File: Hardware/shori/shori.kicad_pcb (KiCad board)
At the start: 4 copper layers, 106 x 44.8 mm, 134 parts, among them J1 430450200, J2 SWD_Header, J3 UART_Header, J4 530480310, J5 Conn_01x03, J6 530480210, J7 GROUND PROBE, SW1 SW_SPDT, U1 CS4272, U2 STM32H750VBTx, U3 NE5532, U4 NE5532, U5 TPS73733DCQR, U6 W25Q128JVS, U7 TLV9001IDCK, U8 MAX40200AUK, Y1 16MHz

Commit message: Shori: Final BOM touches
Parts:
- C15: footprint MyFootprints:CAPPM3216X180N -> Capacitor_SMD:C_1206_3216Metric_Pad1.33x1.80mm_HandSolder
- C19, C35: value 1μF -> 1uF
- C21, C34: value 0.1uF -> 100nF
- moved G*** 0.68 mm to (156.6, 92.9)
- moved C15 0.25 mm to (156.0, 128.5)
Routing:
- net GND: track 67.6 -> 71.6 mm, vias 117 -> 118
- net +5V: track 8.97 -> 9.50 mm

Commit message: Gen: PSU, rev 1 schems done, mae and shori orderd
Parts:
- AUDIO IN: renamed from J4
- AUDIO OUT: renamed from J6
- AUX IN: renamed from J5
- moved H1 2.75 mm to (195.2, 130.5)
- moved H2 2.75 mm to (195.0, 96.0)
- moved GND 2.28 mm to (104.0, 122.2)
- moved H3 1.79 mm to (103.8, 130.5)
- moved H4 1.79 mm to (103.8, 95.8)
- moved C50 1.00 mm to (170.5, 111.8)
- renumbered TP2 to 3V3, TP3 to 3V3A, TP1 to 5V, TP4 to 5VA, J7 to GND, TP5 to MCK, SW1 to P, J1 to POWER, J2 to PROGRAMMING, RST1 to RST, TP6 to TX, J3 to UART
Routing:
- net GND: track 71.6 -> 101.1 mm, vias 118 -> 146
- net +5VA: track 66.7 -> 67.7 mm
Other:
- board size 106 x 44.8 mm -> 101.5 x 44.8 mm

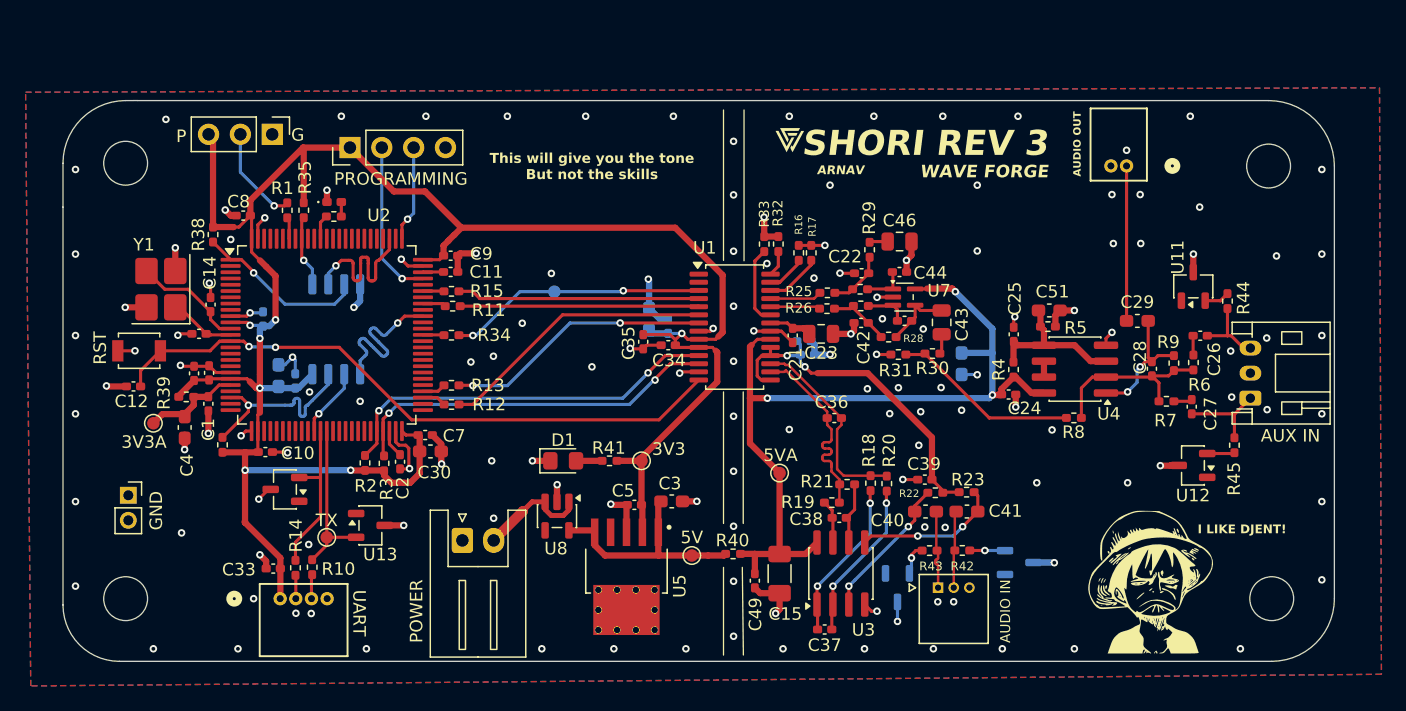
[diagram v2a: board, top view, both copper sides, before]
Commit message: Remvoed 3.3V on shori UART and changed tantalum cap
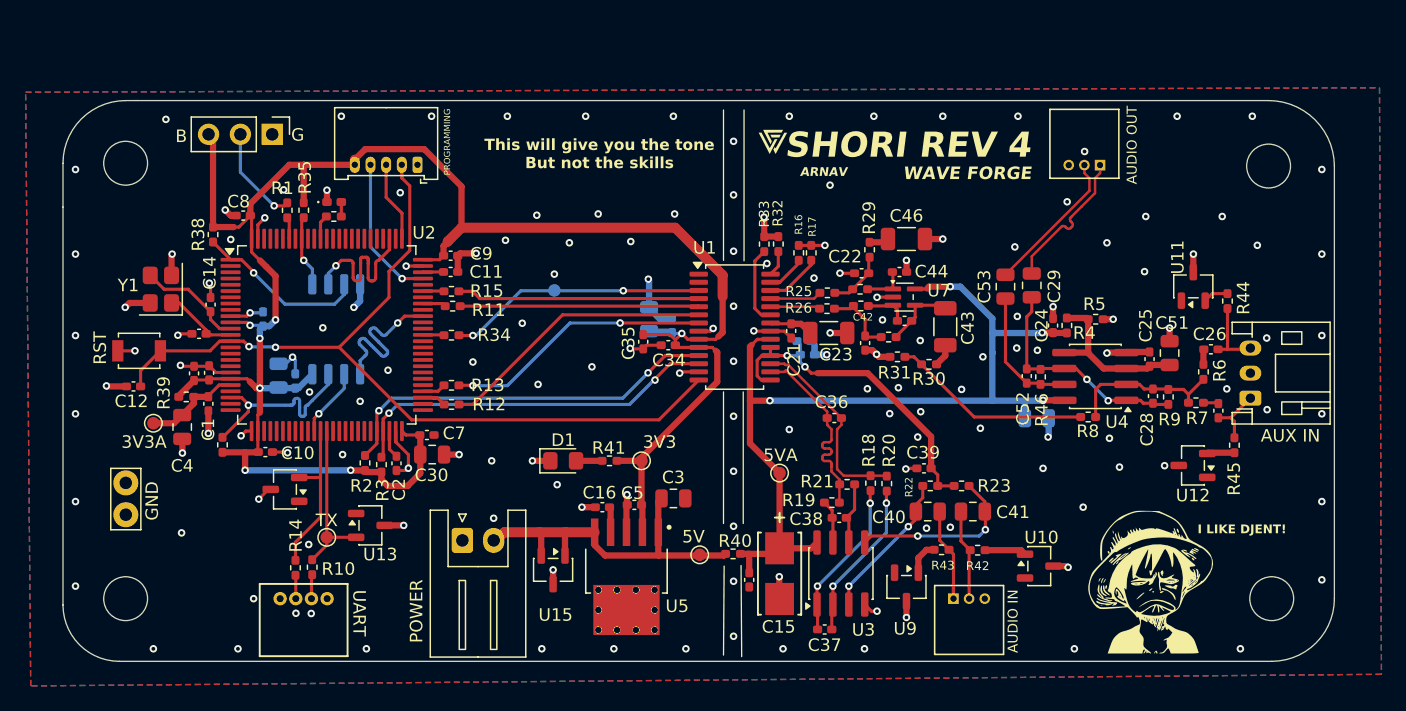
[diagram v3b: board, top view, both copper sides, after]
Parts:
- removed the AUDIO OUT at (183.7, 96.0)
- removed C33: 100nF, Capacitor_SMD:C_0402_1005Metric_Pad0.74x0.62mm_HandSolder
- removed the GND at (104.0, 122.2)
- removed the PROGRAMMING at (121.7, 94.5)
- removed U8: MAX40200AUK, Package_TO_SOT_SMD:SOT-23-5
- added AUDIO OUT: 530480310, MyFootprints:MOLEX_530480310, F.Cu at (181.6, 95.9)
- added C16: 10nF, Capacitor_SMD:C_0402_1005Metric_Pad0.74x0.62mm_HandSolder, F.Cu at (141.8, 123.2)
- added C52: 100pF, Capacitor_SMD:C_0402_1005Metric_Pad0.74x0.62mm_HandSolder, F.Cu at (175.7, 112.7)
- added C53: 10uF, Capacitor_SMD:C_0805_2012Metric, F.Cu at (174.0, 105.6)
- added GND: TestPoint_Bridge_Pitch2.54mm_Drill1.0mm, TestPoint:TestPoint_Bridge_Pitch2.54mm_Drill1.0mm, F.Cu at (103.8, 123.8)
- added PROGRAMMING: Conn_01x05_Pin, Connector_Molex:Molex_PicoBlade_53048-0510_1x05_P1.25mm_Horizontal, F.Cu at (127.1, 95.9)
- added R46: 10K, Resistor_SMD:R_0402_1005Metric_Pad0.72x0.64mm_HandSolder, F.Cu at (176.8, 112.8)
- added U15: ~, Package_TO_SOT_SMD:SOT-23-3, F.Cu at (137.9, 128.2)
- C15: value 100uF -> 47uF; footprint Capacitor_SMD:C_1206_3216Metric_Pad1.33x1.80mm_HandSolder -> MyFootprints:CAPMP6.3X3.2_2.8N_KEM
- C17, C29, C3, C30, C4, C40, C41, C47, C50, C51: footprint Capacitor_SMD:C_0603_1608Metric_Pad1.08x0.95mm_HandSolder -> Capacitor_SMD:C_0805_2012Metric
- C23, C43, C46: footprint Capacitor_SMD:C_0805_2012Metric -> Capacitor_SMD:C_1206_3216Metric
- U10, U9: moved to F.Cu
- Y1: value 16MHz -> 12.288MHz; footprint Crystal:Crystal_SMD_3225-4Pin_3.2x2.5mm_HandSoldering -> Crystal:Crystal_SMD_3225-4Pin_3.2x2.5mm
- moved C25 11.0 mm to (185.5, 111.4)
- moved C51 10.2 mm to (187.1, 110.9), turned to -90 degrees
- moved C29 8.89 mm to (176.1, 105.5), turned to 90 degrees
- moved C50 7.41 mm to (176.5, 116.1), turned to 180 degrees
- moved C24 6.55 mm to (177.8, 108.7), turned to 90 degrees
- moved R4 5.52 mm to (178.9, 108.7)
- moved R5 3.86 mm to (181.2, 108.2)
- moved R9 2.74 mm to (187.0, 114.4), turned to -90 degrees
- moved R7 2.36 mm to (189.2, 114.9)
- moved C28 2.18 mm to (185.8, 114.3), turned to -90 degrees
- moved C27 2.15 mm to (191.0, 115.5)
- moved U4 1.73 mm to (181.2, 112.8)
- moved C42 1.64 mm to (162.8, 110.1), turned to 90 degrees
- moved U10 1.62 mm to (176.7, 127.9)
- moved AUDIO IN 1.51 mm to (169.8, 130.5)
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- renumbered P to B, MCK to TP5
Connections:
- 5V pad 1: /5V_PROTECTED -> +5V
- C28 pad 2: /SUMMED_OUT -> /SUMMED_OUT+
- C29 pad 1: /SUMMED_OUT -> /SUMMED_OUT+
- C29 pad 2: /AUDIO_OUT -> /AUDIO_OUT+
- C3 pad 1: /5V_PROTECTED -> +5V
- R40 pad 2: /5V_PROTECTED -> +5V
- R9 pad 2: /SUMMED_OUT -> /SUMMED_OUT+
- U10 pad 1: unconnected-(U10-IO1-Pad1) -> /SHUNT_RES_AINM
- U10 pad 2: /SHUNT_RES_AINM -> unconnected-(U10-IO2-Pad2)
- U4 pad 1: /SUMMED_OUT -> /SUMMED_OUT+
- U4 pad 6: /UNUSED_INVERTOR -> /SUMMED_OUT+
- U4 pad 7: /UNUSED_INVERTOR -> /SUMMED_OUT-
- U5 pad 1: /5V_PROTECTED -> +5V
- U5 pad 4: unconnected-(U5-NR/FB-Pad4) -> Net-(U5-NR/FB)
- U5 pad 5: /5V_PROTECTED -> +5V
- U9 pad 1: unconnected-(U9-IO1-Pad1) -> /SHUNT_RES_AINP
- U9 pad 2: /SHUNT_RES_AINP -> unconnected-(U9-IO2-Pad2)
- UART pad 1: +3.3V -> GND
- UART pad 4: GND -> unconnected-(J3-Pin_4-Pad4)
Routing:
- net +5V: track 9.27 -> 29.7 mm
- net /5V_PROTECTED: track 20.0 -> 0.00 mm
- net /SUMMED_OUT+: track 0.00 -> 18.4 mm, vias 0 -> 2
- net /NRST: track 50.7 -> 67.9 mm
- net /AUDIO_OUT: track 12.4 -> 0.00 mm
- net /AUDIO_OUT-: track 0.00 -> 11.7 mm
- net /AUDIO_OUT+: track 0.00 -> 11.7 mm
- net /SUMMED_OUT: track 10.6 -> 0.00 mm, vias 2 -> 0
- net /SUMMED_OUT-: track 0.00 -> 10.5 mm
- net +3.3V: track 172.9 -> 162.4 mm
- net GND: track 101.1 -> 93.0 mm, vias 146 -> 158
- net +5VA: track 67.7 -> 73.8 mm, vias 3 -> 4
- net Net-(U3B-+): track 11.7 -> 14.1 mm
- net /JACKR: track 7.12 -> 4.92 mm
- net Net-(U5-NR/FB): track 0.00 -> 2.04 mm
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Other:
- board text added: "SHORI REV 4"
- board text removed: "SHORI REV 3"

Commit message: New Gallery Images for Reddit
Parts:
- renumbered 3V3 to 3.3V, 5V to TP1, 3V3A to TP3
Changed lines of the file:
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@@
 		(filling no)
 		(pcbplotparams
-			(layerselection 0x00000000_00000000_55555555_5755f5ff)
+			(layerselection 0x00000000_00000000_55555555_57555575)
 			(plot_on_all_layers_selection 0x00000000_00000000_00000000_00000000)
 			(disableapertmacros no)
@@
 			(plotframeref no)
 			(mode 1)
-			(useauxorigin no)
+			(useauxorigin yes)
 			(pdf_front_fp_property_popups yes)
 			(pdf_back_fp_property_popups yes)
@@
 			(crossoutdnponfab yes)
 			(subtractmaskfromsilk no)
-			(outputformat 1)
+			(outputformat 4)
 			(mirror no)
 			(drillshape 0)
 			(scaleselection 1)
-			(outputdirectory "Fabrication/")
+			(outputdirectory "../../Galery/Boards/Shori/")
 		)
 	)
@@
 		(descr "SMD pad as test Point, diameter 1.0mm")
 		(tags "test point SMD pad")
-		(property "Reference" "3V3A"
+		(property "Reference" "TP3"
 			(at -0.75 1.5 0)
 			(layer "F.SilkS")
@@
 		(descr "SMD pad as test Point, diameter 1.0mm")
 		(tags "test point SMD pad")
-		(property "Reference" "5V"
+		(property "Reference" "TP1"
 			(at -0.5 -1.448 0)
 			(layer "F.SilkS")
@@
 		(descr "SMD pad as test Point, diameter 1.0mm")
 		(tags "test point SMD pad")
-		(property "Reference" "3V3"
+		(property "Reference" "3.3V"
 			(at 1.445716 -1.5 180)
 			(layer "F.SilkS")
@@
 		(polygon
 			(pts
-				(xy 95.802428 90.081923) (xy 203.851607 89.727761) (xy 204.00503 136.53443) (xy 96.210899 137.463709)
+				(xy 95.759282 85.077134) (xy 203.835202 84.722884) (xy 204.00503 136.53443) (xy 96.210899 137.463709)
 			)
 		)
